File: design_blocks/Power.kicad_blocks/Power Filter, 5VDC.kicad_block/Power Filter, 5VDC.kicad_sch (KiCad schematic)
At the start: 7 parts

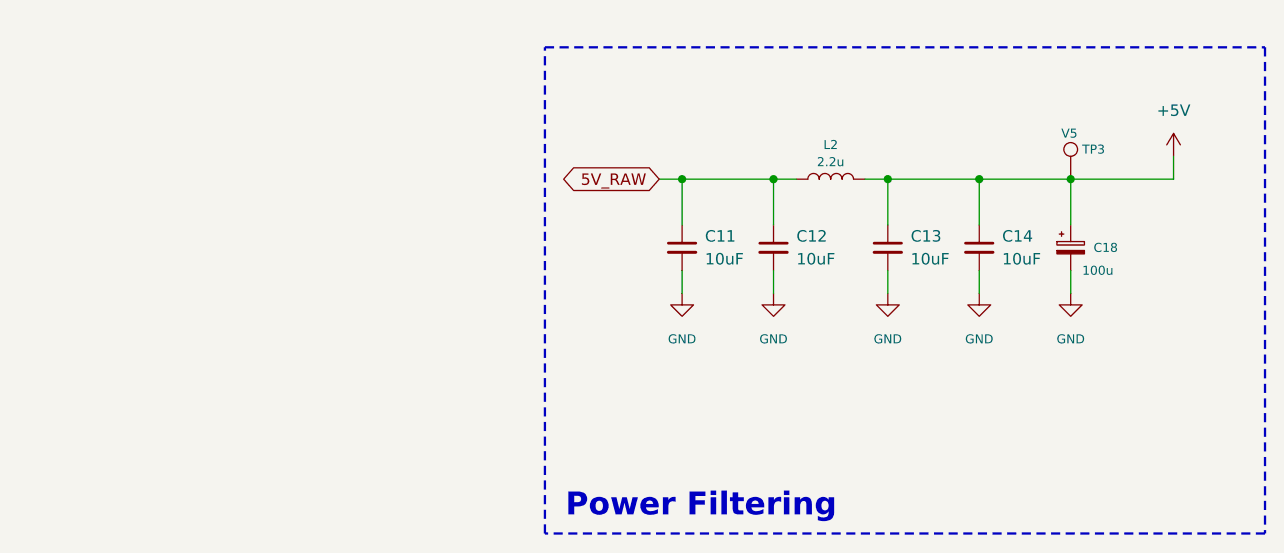
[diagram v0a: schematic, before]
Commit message: Added additional parts; fixed origin of other parts
Added new design blocks
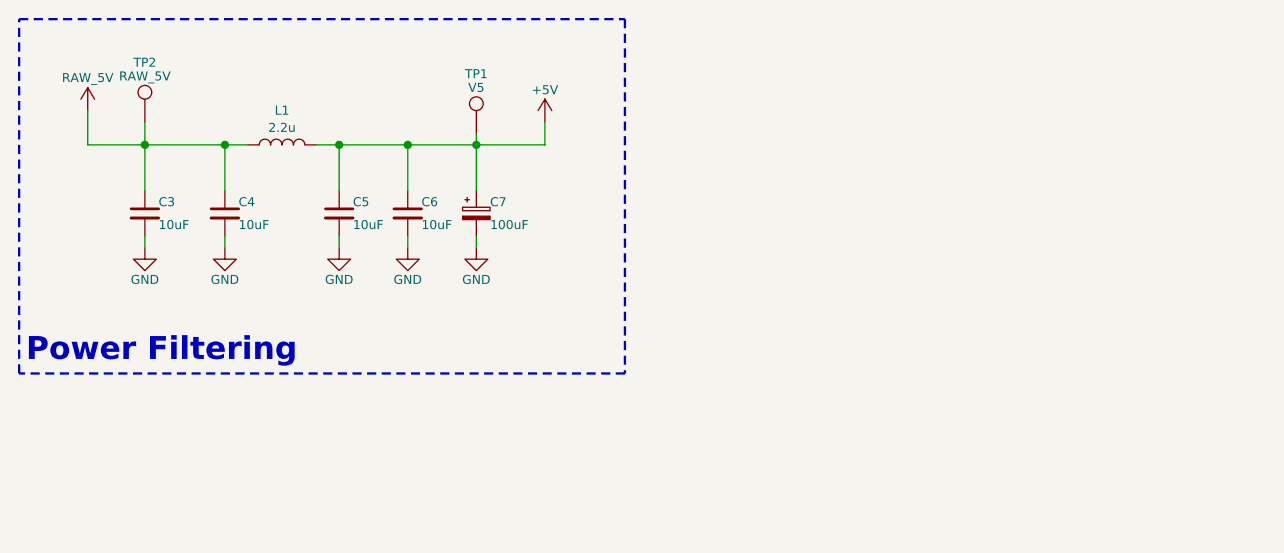
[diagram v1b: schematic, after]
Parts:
- added TP2: RAW_5V, TestPoint:TestPoint_Pad_D1.0mm, symbol Connector:TestPoint
- C3: renamed from C11; MN (none) -> Samsung
- C4: renamed from C12; MN (none) -> Samsung
- C5: renamed from C13; MN (none) -> Samsung
- C6: renamed from C14; MN (none) -> Samsung
- C7: renamed from C18; value 100u -> 100uF; FT Rotation Offset (none) -> 180; JLCPCB C3339 -> (none); MN (none) -> Honor Elec; MPN (none) -> RVT1V101M0607
- L1: renamed from L2; JLCPCB C408335 -> (none); LCSC C408335 -> C438930; MN Sunlord -> Cybermax; MPN MWSA0402S-2R2MT -> CMLO0420H2R2MTT
- TP1: renamed from TP3; footprint TestPoint:TestPoint_Pad_D2.0mm -> TestPoint:TestPoint_Pad_D1.0mm; now left out of the parts list
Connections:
- net 5V_RAW renamed RAW_5V
- net RAW_5V: now also TP2.1
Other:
- moved on the sheet: C3, C4, C5, C6, C7, L1, TP1
